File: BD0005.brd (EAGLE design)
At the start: 67.3 x 33 mm, 68 parts, among them J1 1050171001, J3 HEADER_1X3FEMALE, J4 HEADER_1X3FEMALE, U1 ATSAMD11D14A-MNT, U2 AP2114H-3.3TRG1, X1 MC-146-32.7680JKA-A0:ROHS

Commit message: initial updates from v1. (not sure what was changed)
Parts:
- removed CR1: USBLC6-2P6SOT-666-M, Clock:SOT-666-M
- removed JP2: (no value), adafruit:1X03
- added J2: HEADER_1X3, DroidForge:1X03-CLEANBIG
- B1, B2: device Clock:4-SMD_BUTTON -> DroidForge:4-SMD_BUTTON
- C1, C2: device adafruit:C0805 -> DroidForge:0402
- C10, C11, C12, C13, C14, C15, C16, C17, C18, C19, C20, C21, C22, C23, C24, C25, C3, C4, C5, C6, C7, C8, C9: device adafruit:C0402 -> DroidForge:0402
- J1: value 1050171001 -> CONN_MICROUSB_FEMALE; device Clock:CON00679_5 -> DroidForge:CON00679_5
- J3, J4: device Clock:F3SMD -> DroidForge:F3SMD_RIGHTANGLE
- JP1: value PINHD-1X10 -> HEADER_1X10; device adafruit:1X10-BIG -> DroidForge:1X10-BIG
- L1, L10, L11, L12, L13, L14, L15, L16, L17, L18, L19, L2, L20, L3, L4, L5, L6, L7, L8, L9: value WS2812B -> WS2812B-B; device Clock:SK6812 -> DroidForge:SK6812-B
- R1, R3: device adafruit:R0402 -> DroidForge:0402
- R2: value 3352T-1-104LF -> POT_THUMBWHEEL_3352T-1-104LF; device Clock:THUMBWHEEL -> DroidForge:THUMBWHEEL
- TP1, TP2, TP3, TP4, TP5, TP6, TP7, TP8, TP9: device Clock:TEST_POINT -> DroidForge:TEST_POINT
- U1: value ATSAMD11D14A-MNT -> SAMD11D14A; device Clock:QFN24_4X4MC -> DroidForge:QFN24_4X4MC
- U2: device Clock:SOT-223 -> DroidForge:SOT-223
- X1: device Clock:4-SMD_FLAT_LEADS -> DroidForge:4-SMD_FLAT_LEADS
- moved R3 1.45 mm to (44.2, 8.41), turned to 0 degrees
- moved C4 0.41 mm to (33.2, 9.88)
- moved X1 0.25 mm to (30.7, 11.3)
- moved C5 0.25 mm to (33.2, 12.7)
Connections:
- removed net N$1: CR1.3, J1.3
- removed net N$3: CR1.1, J1.2
- net BIN: now also R3.P$2; no longer R3.2
- net GND: now also C1.P$2, C10.P$2, C11.P$2, C12.P$2, C13.P$2, C14.P$2, C15.P$2, C16.P$2, C17.P$2, C18.P$2, C19.P$2, C2.P$2, C20.P$2, C21.P$2, C22.P$2, C23.P$2, C24.P$2, C25.P$2, C3.P$2, C4.P$2, C5.P$2, C6.P$2, C7.P$2, C8.P$2, C9.P$2, J2.2, R3.P$1; no longer C1.2, C10.2, C11.2, C12.2, C13.2, C14.2, C15.2, C16.2, C17.2, C18.2, C19.2, C2.2, C20.2, C21.2, C22.2, C23.2, C24.2, C25.2, C3.2, C4.2, C5.2, C6.2, C7.2, C8.2, C9.2, CR1.2, JP2.2, R3.1
- net N$4: now also C4.P$1; no longer C4.1
- net N$5: now also C5.P$1; no longer C5.1
- net RESET: now also R1.P$1; no longer R1.1
- net USB_D+: now also J1.3; no longer CR1.4
- net USB_D-: now also J1.2; no longer CR1.6
- net VCC: now also C10.P$1, C11.P$1, C12.P$1, C13.P$1, C14.P$1, C15.P$1, C16.P$1, C17.P$1, C18.P$1, C19.P$1, C2.P$1, C20.P$1, C21.P$1, C22.P$1, C23.P$1, C24.P$1, C25.P$1, C3.P$1, C6.P$1, C7.P$1, C8.P$1, C9.P$1, J2.1, R1.P$2, U2.4; no longer C10.1, C11.1, C12.1, C13.1, C14.1, C15.1, C16.1, C17.1, C18.1, C19.1, C2.1, C20.1, C21.1, C22.1, C23.1, C24.1, C25.1, C3.1, C6.1, C7.1, C8.1, C9.1, CR1.5, JP2.1, R1.2
- net VIN: now also C1.P$1, J2.3; no longer C1.1, JP2.3
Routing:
- net N$3: track 19.7 -> 0.00 mm
- net N$1: track 19.2 -> 0.00 mm
- net USB_D-: track 4.74 -> 23.0 mm
- net USB_D+: track 5.51 -> 23.2 mm
- net VCC: track 366.8 -> 350.6 mm
- net A5: track 32.2 -> 34.1 mm
- net GND: vias 23 -> 24

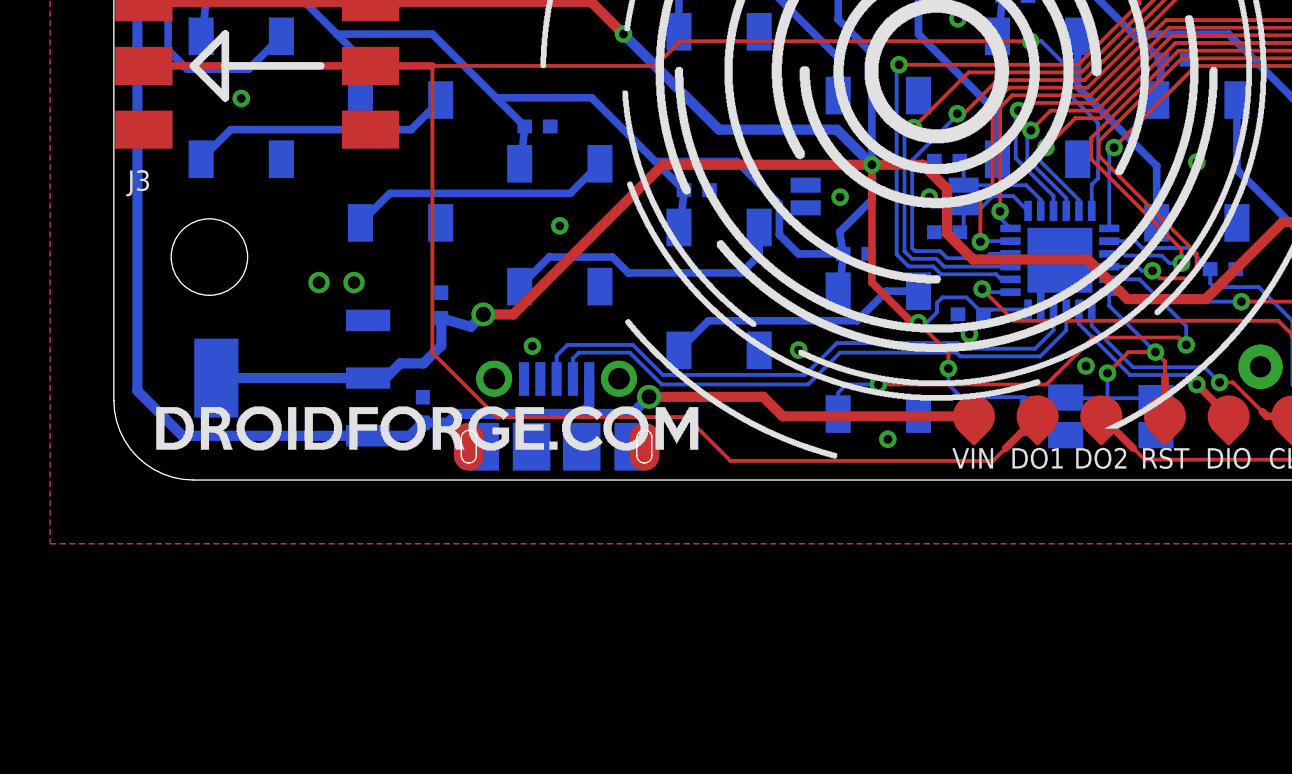
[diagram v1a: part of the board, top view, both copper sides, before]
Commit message: changed SAMD11 to SAMD21E (in process)
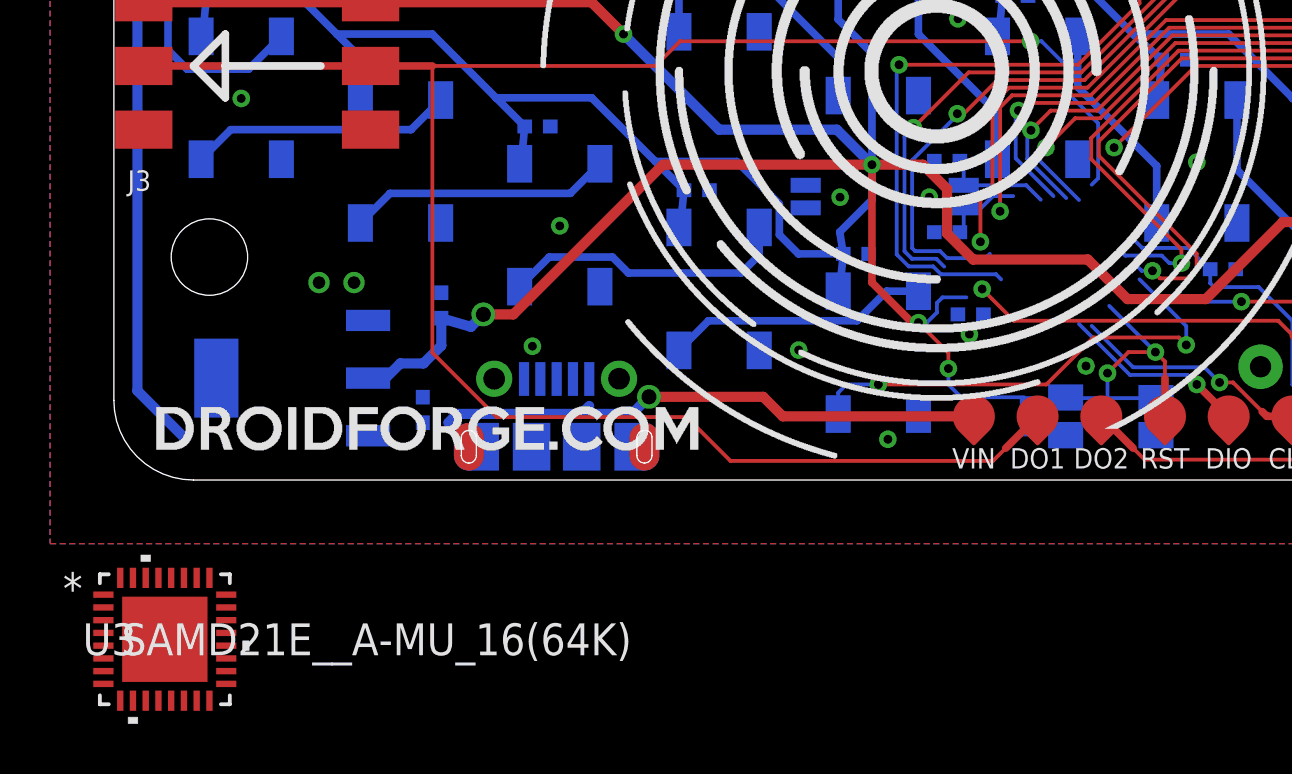
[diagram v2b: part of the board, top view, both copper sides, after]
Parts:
- removed U1: SAMD11D14A, DroidForge:QFN24_4X4MC
- added U3: SAMD21E__A-MU_16(64K), DroidForge:QFN32_5X5MC_MCH
- B1, B2: value EVQ-P7A01P -> SWITCH_EVQ-P7A01P
- U2: value AP2114H-3.3TRG1 -> REG_AP2114H-3.3TRG1
- X1: value MC-146-32.7680JKA-A0:ROHS -> XTAL_MC-146-32.7680JKA-A0:ROHS
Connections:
- removed net USB_D+: J1.3, U1.22
- removed net USB_D-: J1.2, U1.21
- new net A10: U3.13
- new net A11: U3.14
- new net A16: U3.17
- new net A17: U3.18
- new net A18: U3.19
- new net A19: U3.20
- new net A22: U3.21
- new net A23: U3.22
- new net A24: U3.23
- new net A25: U3.24
- new net A27: U3.25
- new net A28: U3.27
- new net A30: U3.31
- new net A31: U3.32
- new net A8: U3.11
- new net A9: U3.12
- new net D+: J1.3
- new net D-: J1.2
- new net VDDANA: U3.9
- new net VDDCORE: U3.29
- new net VDDIN: U3.30
- net A2: now also U3.3; no longer U1.1
- net A3: now also U3.4; no longer U1.2
- net A4: now also U3.5; no longer U1.3
- net A5: now also U3.6; no longer U1.4
- net A6: now also U3.7; no longer U1.5
- net A7: now also U3.8; no longer U1.6
- net BIN: no longer U1.14
- net DIN: no longer U1.17
- net DOUT_1: no longer U1.12
- net DOUT_2: no longer U1.13
- net GND: now also U3.10, U3.28, U3.33; no longer C3.P$2, U1.23, U1.25
- net MISO: no longer U1.11
- net MOSI: no longer U1.9
- net N$4: now also U3.1; no longer U1.7
- net N$5: now also U3.2; no longer U1.8
- net RESET: no longer U1.18
- net SCK: no longer U1.10
- net SCL: no longer U1.16
- net SDA: no longer U1.15
- net SWCLK: no longer U1.19
- net SWDIO: no longer U1.20
- net VCC: no longer C3.P$1, U1.24
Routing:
- net USB_D+: track 23.2 -> 0.00 mm
- net USB_D-: track 23.0 -> 0.00 mm
- net VIN: track 75.6 -> 63.7 mm
- net VCC: track 350.6 -> 340.8 mm
- net DOUT_2: track 78.6 -> 75.6 mm
- net A4: track 34.0 -> 31.4 mm
- net GND: track 2.28 -> 0.00 mm
- net DIN: track 31.5 -> 30.3 mm
- net A6: track 30.4 -> 29.3 mm
- net SCL: track 42.3 -> 41.2 mm
- net DOUT_1: track 82.1 -> 81.0 mm
- net BIN: track 23.8 -> 22.7 mm
- net A2: track 16.1 -> 15.1 mm
- net N$4: track 4.04 -> 3.20 mm
- net A5: track 34.1 -> 33.2 mm
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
